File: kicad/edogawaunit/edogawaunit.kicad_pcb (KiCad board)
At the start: 2 copper layers, 26.7 x 31.8 mm, 11 parts, among them J1 Conn_01x03, J2 Conn_01x02, J3 Conn_01x02, SW1 SW_Push, U1 TLP222A-2

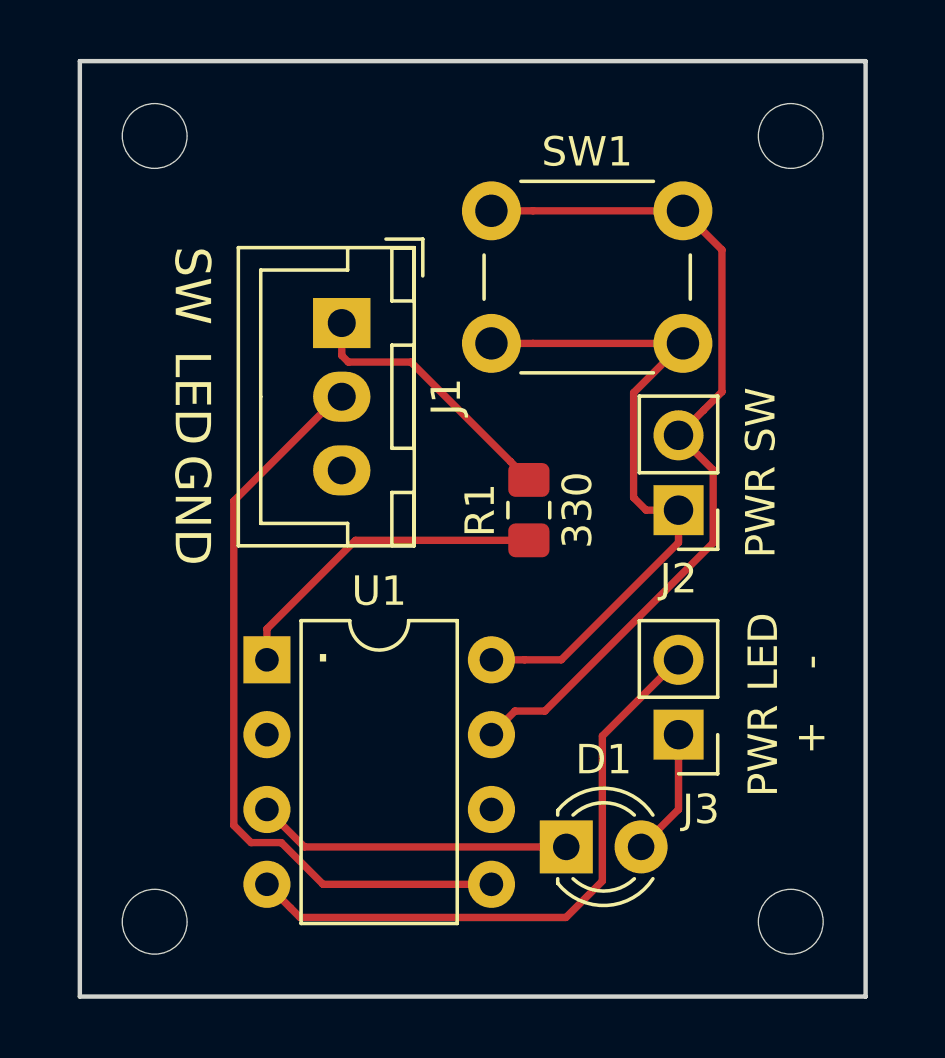
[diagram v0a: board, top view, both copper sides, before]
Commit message: EdogawaUnit shrinked
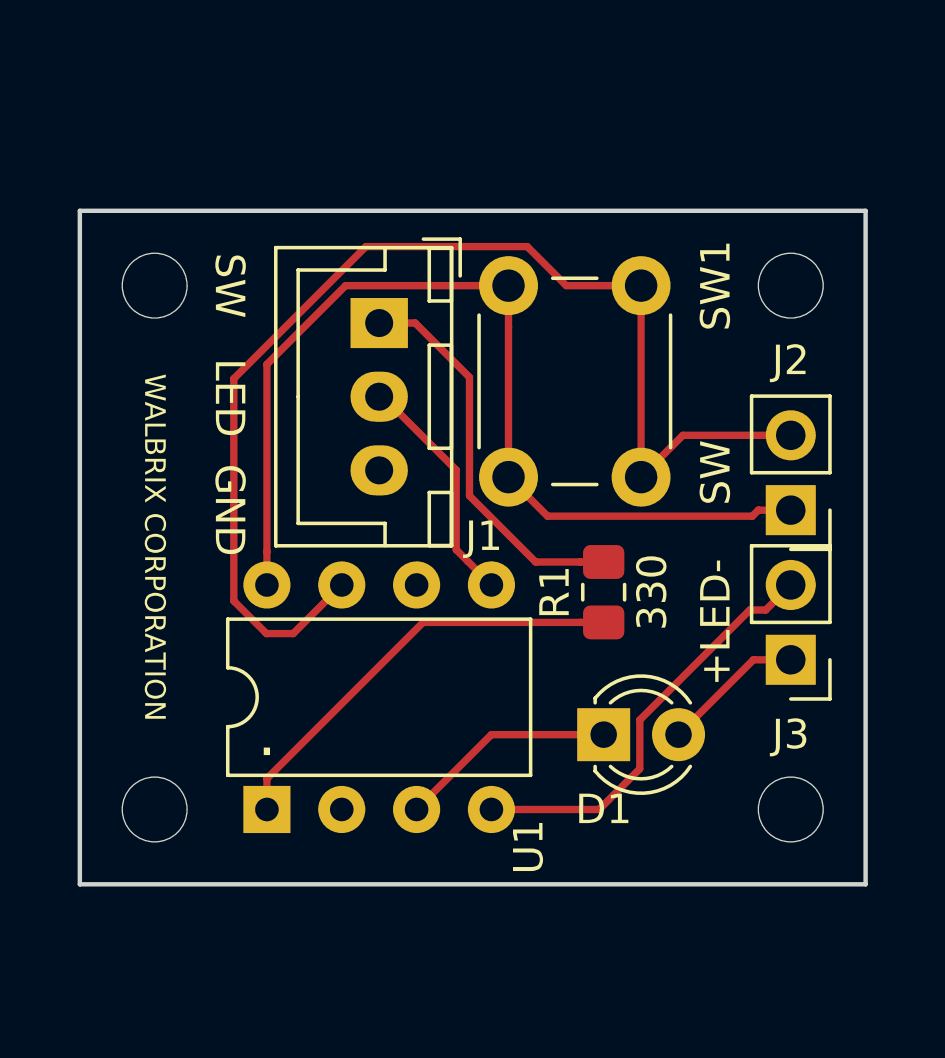
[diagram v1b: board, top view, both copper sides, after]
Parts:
- moved SW1 5.68 mm to (157.5, 97.8), turned to 270 degrees
- moved REF** 5.08 mm to (141.0, 97.8)
- moved REF** 5.08 mm to (162.6, 97.8)
- moved U1 5.08 mm to (144.8, 115.6), turned to 90 degrees
- moved J3 4.58 mm to (162.6, 110.5)
- moved D1 4.02 mm to (156.2, 113.0)
- moved J2 3.81 mm to (162.6, 105.4)
- moved REF** 3.81 mm to (162.6, 115.6)
- moved REF** 3.81 mm to (141.0, 115.6)
- moved R1 3.77 mm to (156.2, 108.2)
- moved J1 1.27 mm to (148.6, 99.1)
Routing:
- net /LED_IN: track 25.7 -> 8.04 mm
- net /SW2: track 29.6 -> 40.7 mm
- net /SW1: track 23.2 -> 33.5 mm
- net /LEDMINUS: track 20.9 -> 14.3 mm
- net /SW_OUT: track 9.20 -> 13.3 mm
- net Net-(R1-Pad1): track 11.2 -> 14.7 mm
- net Net-(D1-Pad1): track 10.7 -> 7.40 mm
- removed copper zone on F.Cu, net GND
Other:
- board size 26.7 x 31.8 mm -> 26.7 x 22.9 mm
- board text added: "+LED-"
- board text added: "WALBRIX CORPORATION"
- board text removed: "PWR LED + -"
- board text removed: "PWR SW"

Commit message: PCBs update
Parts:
- REF** (x4): value MountingHole_2.2mm_M2 -> MountingHole_3mm; footprint MountingHole:MountingHole_2.2mm_M2 -> MountingHole:MountingHole_3mm
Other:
- board size 26.7 x 22.9 mm -> 27.9 x 24.1 mm
